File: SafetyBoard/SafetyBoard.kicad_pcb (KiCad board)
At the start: 4 copper layers, 157 x 104 mm, 170 parts, among them J1 Estop, J10 TSSI, J11 ACCU, J12 BBC, J13 614004135023, J14 footwell, J15 RTD B, J16 Brakelight, J17 SHOCK/WHEEL SNSR, J18 39306207, J19 AMP, J2 TS ON SW, J3 SDC OUT, J4 ACCU, J5 12v EXP, J6 PWR IN, J7 24v EXP, J8 5v EXP, J9 Current Sensor, K1 G6B-2214P-US DC12, K2 G6B-2214P-US DC12, K3 G6B-2214P-US DC12, Q1 IRLIZ44N NMOS, Q2 IRLIZ44N NMOS, Q3 IRLIZ44N NMOS, Q4 IRLIZ44N NMOS, Q5 PMOS IRF9540, Q6 PMOS IRF9540, Q7 PMOS IRF9540, SW1 SW_Push, SW2 SW_Push, SW3 SW_Push, U1 40106 Inverter, U2 4081 AND Gate, U3 LT1084-5.0, U4 LM393, U5 LM393, U6 CD4071BE OR Gate, U7 LM393, U8 LM555xN, U9 OKX-T/5-D12N-C

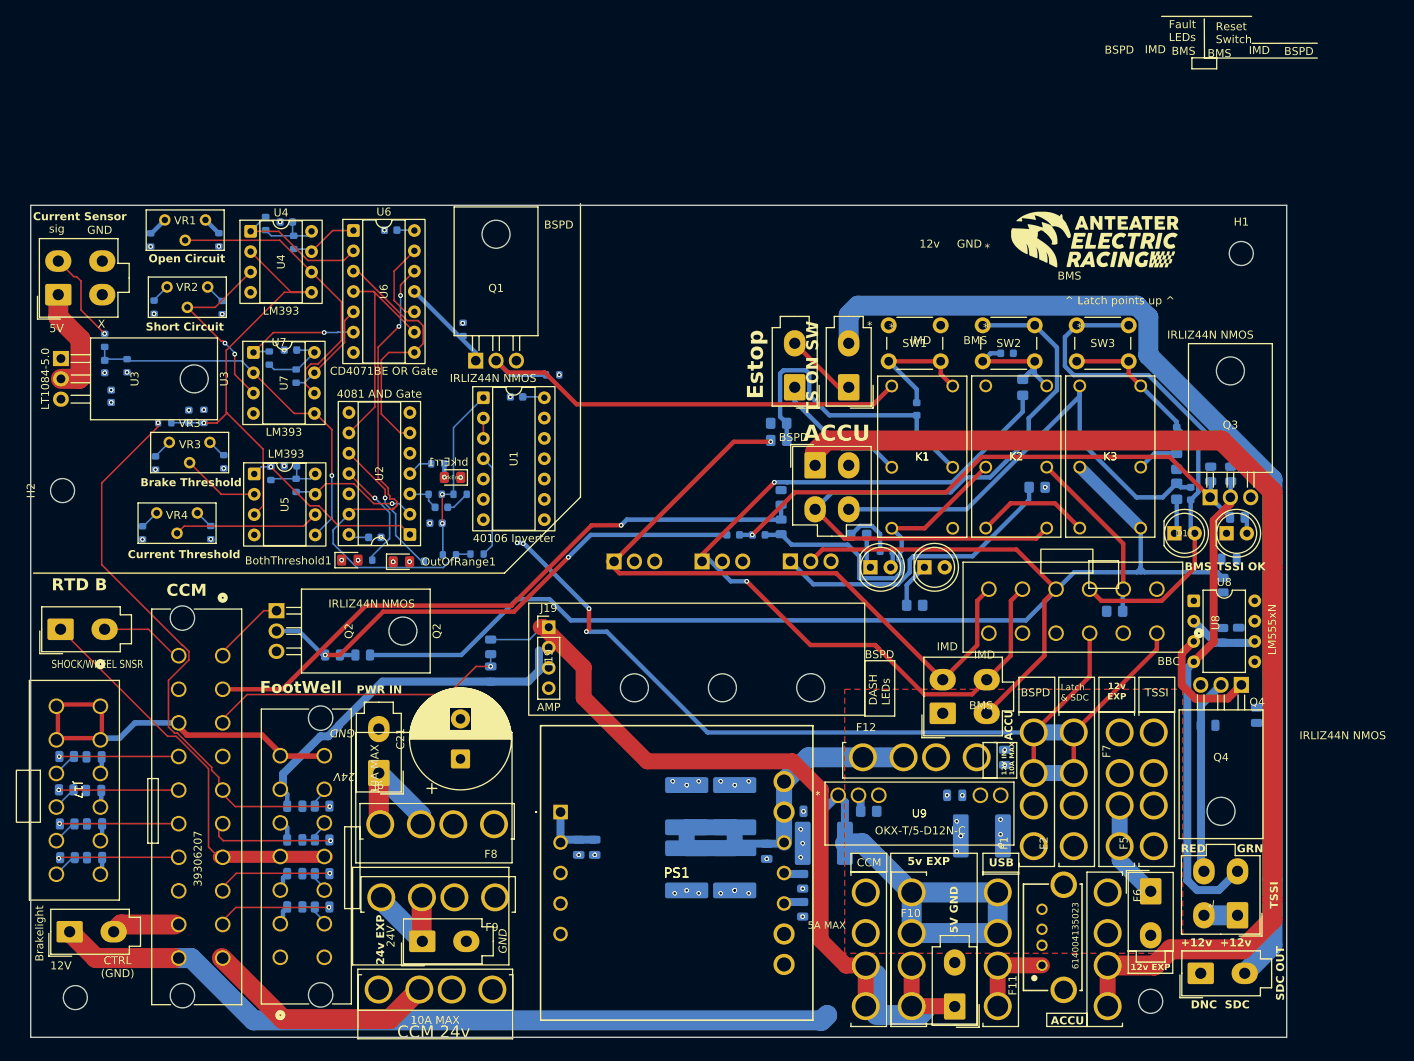
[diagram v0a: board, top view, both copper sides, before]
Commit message: Redimensioned, New Layout
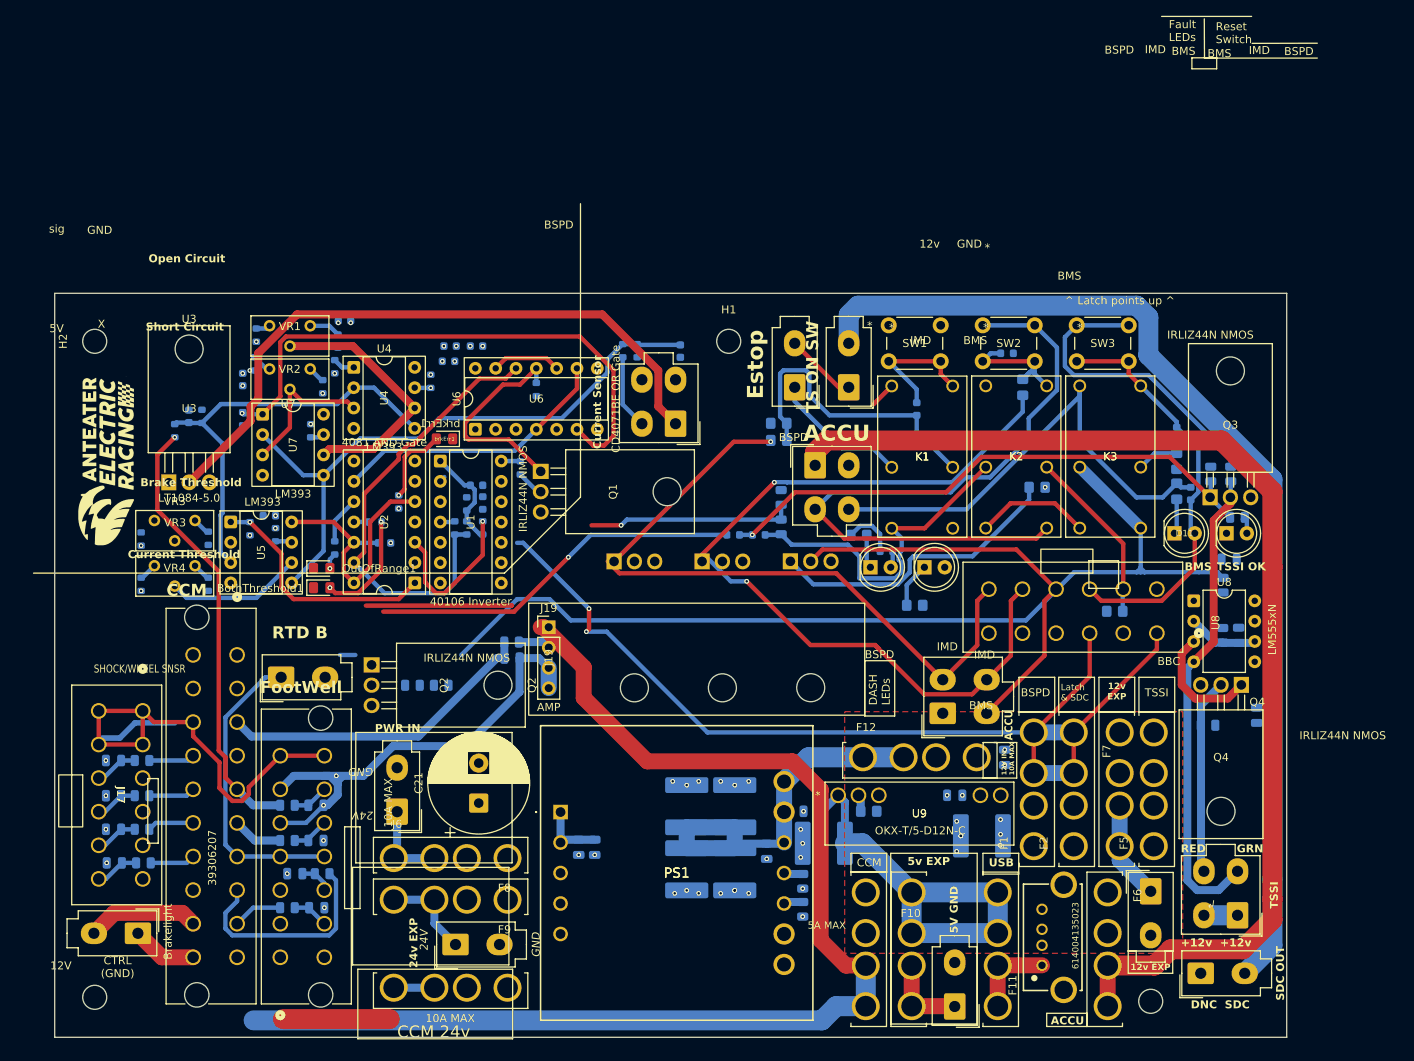
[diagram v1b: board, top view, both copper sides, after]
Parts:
- moved J9 78.8 mm to (146.6, 86.3), turned to 180 degrees
- moved C3 72.0 mm to (147.2, 77.2)
- moved H1 65.0 mm to (153.2, 76.0)
- moved R5 64.8 mm to (140.0, 77.2), turned to -90 degrees
- moved R2 63.8 mm to (141.8, 77.2)
- moved C1 46.1 mm to (121.7, 76.6), turned to 180 degrees
- moved U6 29.1 mm to (121.6, 87.0), turned to 90 degrees
- moved J15 28.2 mm to (97.3, 118.0)
- moved R19 24.4 mm to (116.0, 81.0)
- moved U4 21.3 mm to (106.4, 79.3)
- moved U3 20.5 mm to (83.3, 93.6), turned to 0 degrees
- moved R18 19.9 mm to (104.0, 79.2)
- moved R9 19.5 mm to (104.4, 76.0)
- moved H2 19.1 mm to (74.0, 76.0)
- moved VR1 18.6 mm to (100.9, 74.1)
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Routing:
- net +5V: track 14.0 -> 82.2 mm
- net /BSPD/PEDAL_SHORT: track 15.6 -> 70.3 mm
- net /BSPD/BSPD_FAULT: track 66.4 -> 13.4 mm
- net /CCM Helper/CCM fdbk: track 81.0 -> 44.1 mm
- net /BSPD/CURRENT: track 47.8 -> 77.2 mm, vias 1 -> 0
- net /CCM Helper/24V: track 53.6 -> 26.7 mm
- net /BSPD/PEDAL_OPEN: track 12.4 -> 31.8 mm
- net GND: track 18.5 -> 0.00 mm, vias 47 -> 34
- net /BSPD/B_IN: track 72.1 -> 55.2 mm, vias 2 -> 1
- net Net-(D3-A): track 63.8 -> 46.9 mm, vias 2 -> 1
- net /CCM Helper/12V: track 177.1 -> 161.9 mm
- net Net-(D1-K): track 4.32 -> 19.5 mm, vias 0 -> 1
- net /BSPD/FAULT_SENSED: track 11.8 -> 26.5 mm
- net Net-(BothThreshold1-A): track 0.13 -> 13.9 mm, vias 1 -> 2
- net /CCM Helper/CCM3v3: track 50.9 -> 37.9 mm
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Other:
- board size 157 x 104 mm -> 154 x 93 mm

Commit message: Traces Check 1
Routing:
- net /BSPD/BSPD_FAULT: track 13.4 -> 77.0 mm, vias 0 -> 1
- net /CCM Helper/CCM fdbk: track 44.1 -> 80.3 mm
- net /CCM Helper/TSSI BYP: track 0.00 -> 17.3 mm
- net +12V: track 338.4 -> 354.9 mm, vias 17 -> 18
- net /CCM Helper/12V: track 161.9 -> 172.2 mm
- net Net-(D3-A): track 46.9 -> 56.4 mm
- net Net-(Q6-G): track 50.5 -> 52.4 mm
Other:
- outline, holes or cut-outs redrawn
- board text added: "NC SDC"
- board text removed: "DNC SDC"

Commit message: Traces Check 2
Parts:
- moved J3 93.3 mm to (154.5, 81.8), turned to 180 degrees
- moved H1 13.0 mm to (154.0, 89.0)
- moved H3 12.0 mm to (218.0, 158.0)
- moved R24 1.15 mm to (91.6, 85.0), turned to 180 degrees
- moved C12 0.25 mm to (219.0, 122.8)
- renumbered BothThreshold1 to BT1, OutOfRange1 to OOR1
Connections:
- C13 pad 1: +12V -> /TSSI/GLV
- F7 pad 1: /12V -> Net-(J5-Pin_1)
- F7 pad 2: Net-(J5-Pin_1) -> /12V
- R26 pad 1: +12V -> /TSSI/GLV
- R32 pad 1: +12V -> /TSSI/GLV
- R33 pad 1: +12V -> /TSSI/GLV
- R35 pad 1: +12V -> /TSSI/GLV
- U8 pad 8: +12V -> /TSSI/GLV
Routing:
- net Net-(J2-Pin_2): track 132.0 -> 16.3 mm
- net +12V: track 354.9 -> 363.7 mm, vias 18 -> 16
- net Net-(U8-CV): track 0.00 -> 5.74 mm
- net /CCM Helper/12V: track 172.2 -> 173.3 mm
- net /BSPD/PEDAL_SHORT: vias 1 -> 0
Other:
- board text added: "10A"
- board text added: "12v EXP 5A"
- board text added: "5V 5A"
- board text added: "BSPD 2A"
- board text added: "CCM 24v 10A"
- board text added: "CCM 5A"
- board text added: "Latch &SDC 5A"
- board text added: "TSSI 2A"
- board text removed: "12v"
- board text removed: "12v EXP"
- board text removed: "CCM 24v"
- board text removed: "CTRL (GND)"
- board text removed: "Fault LEDs"
- board text removed: "Latch & SDC"
- board text removed: "Open Circuit"
- board text removed: "Reset Switch"
- board text removed: "Short Circuit"
- board text removed: "TSSI"
- board text removed: "^ Latch points up ^"
- board text removed: "sig"

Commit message: Male connector models added
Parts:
- J1, J15, J16, J2, J3, J5, J6, J7, J8: footprint 0footprints:Molex_Mini-Fit_Jr_5566-02A_2x01_P4.20mm_Vertical -> footprints:Molex_Mini-Fit_Jr_5566-02A_2x01_P4.20mm_Vertical
- J10, J11, J4, J9: footprint 0footprints:Molex_Mini-Fit_Jr_5566-04A_2x02_P4.20mm_Vertical -> footprints:Molex_Mini-Fit_Jr_5566-04A_2x02_P4.20mm_Vertical

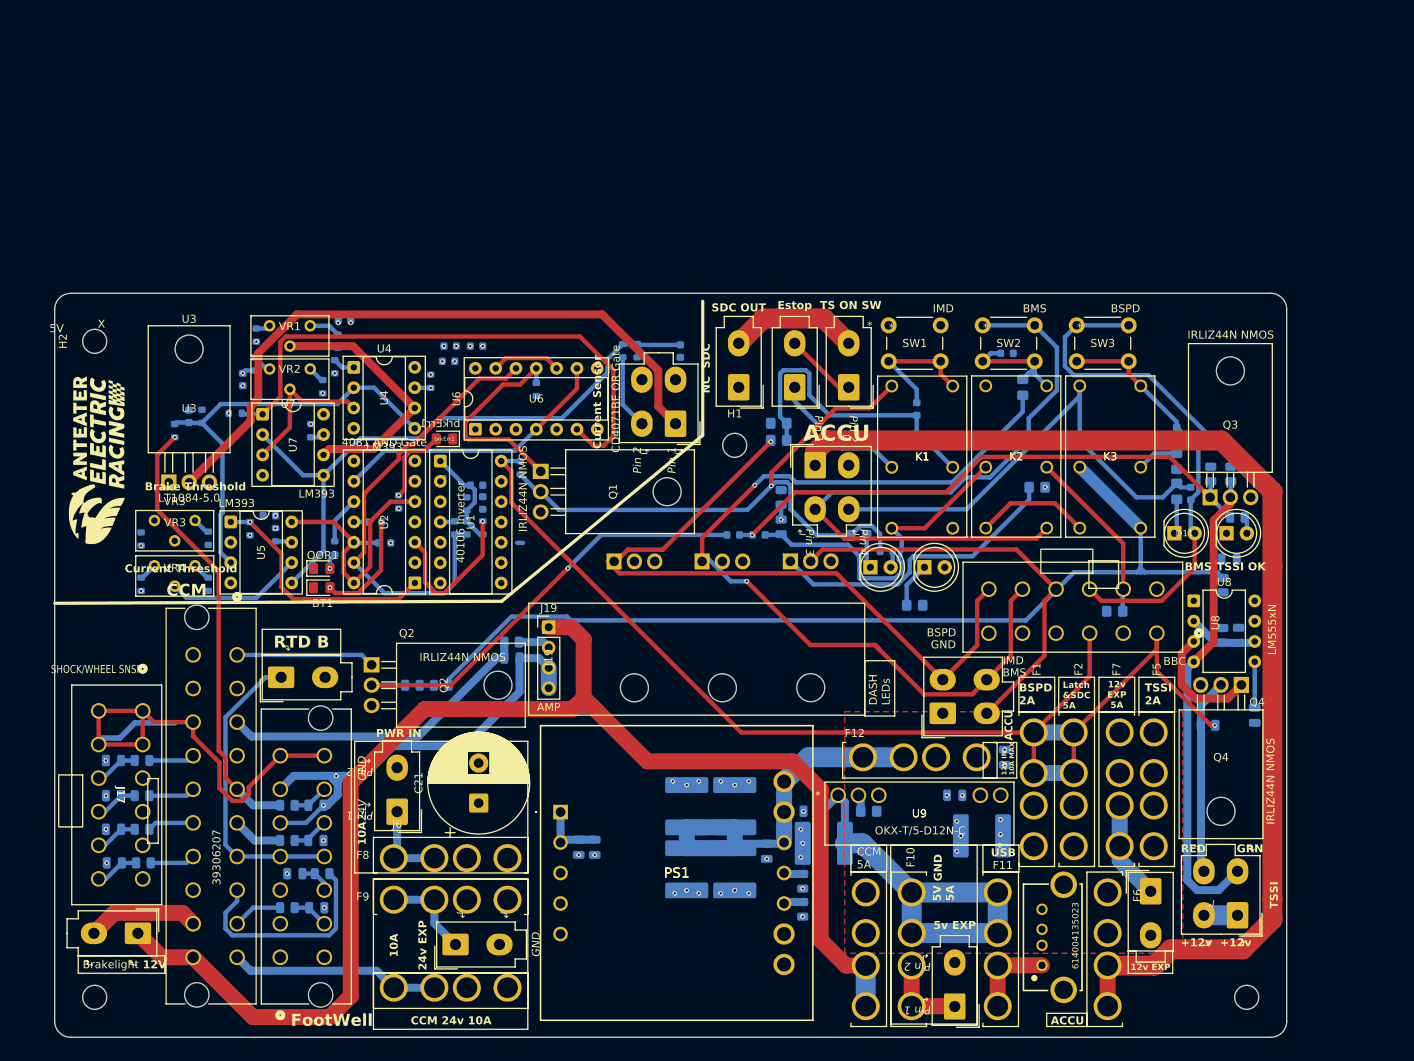
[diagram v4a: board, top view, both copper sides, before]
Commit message: Connector spacing updated
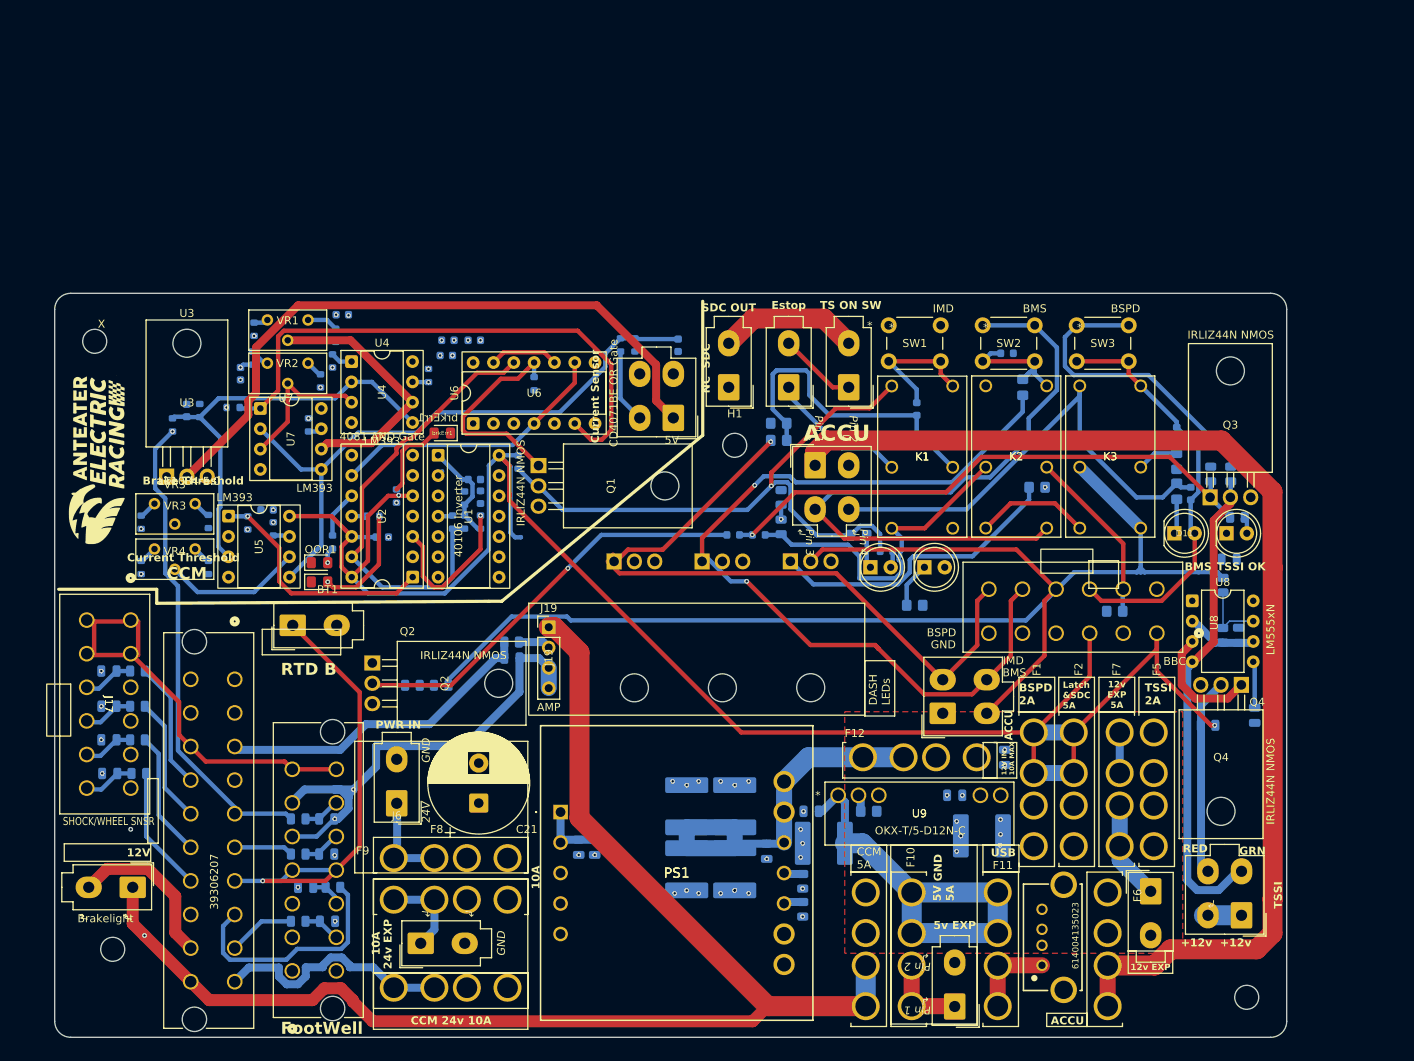
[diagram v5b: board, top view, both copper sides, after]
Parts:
- moved J17 11.4 mm to (78.5, 110.9)
- moved C32 11.2 mm to (75.8, 121.6)
- moved R54 11.2 mm to (79.3, 121.6)
- moved C31 11.2 mm to (75.8, 117.2)
- moved C33 11.2 mm to (75.8, 125.8)
- moved R53 11.2 mm to (79.3, 117.2)
- moved R55 11.2 mm to (79.3, 125.8)
- moved C34 11.2 mm to (75.9, 130.0)
- moved R56 11.2 mm to (79.5, 130.0)
- moved J15 6.66 mm to (98.8, 111.5)
- moved H4 6.41 mm to (76.2, 152.0)
- moved J16 5.79 mm to (78.8, 144.2)
- moved J7 4.35 mm to (114.8, 151.2)
- moved J18 3.06 mm to (91.5, 118.3)
- moved J14 2.27 mm to (98.7, 154.7)
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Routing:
- net +12V: track 363.7 -> 408.6 mm, vias 16 -> 17
- net /CCM Helper/CCM3v3: track 37.9 -> 58.3 mm, vias 0 -> 1
- net /CCM Helper/Wheel/Shock1 OUT: track 5.72 -> 16.0 mm
- net /CCM Helper/Wheel/Shock4 OUT: track 5.63 -> 15.7 mm
- net /CCM Helper/Wheel/Shock3 OUT: track 5.81 -> 15.8 mm
- net /CCM Helper/Wheel/Shock2 OUT: track 5.81 -> 15.8 mm
- net /CCM Helper/5V: track 62.4 -> 53.5 mm
- net Net-(U8-DIS): track 0.00 -> 8.82 mm
- net /CCM Helper/Brakelight: track 14.0 -> 20.5 mm
- net /CCM Helper/12V: track 173.3 -> 167.5 mm, vias 0 -> 1
- net Net-(J5-Pin_1): track 12.3 -> 17.4 mm
- net /CCM Helper/24V: track 26.2 -> 31.1 mm
- net /BSPD/B_IN: track 55.2 -> 60.1 mm
- net /CCM Helper/RTDB: track 18.9 -> 22.7 mm
- net /CCM Helper/APPS1 OUT: track 27.2 -> 29.6 mm
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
